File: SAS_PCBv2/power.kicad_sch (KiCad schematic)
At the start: 18 parts, among them J3 Conn_01x02_Pin, Q2 2N4403, Q3 2N4403, SW1 SW_SPST, U2 LF33_TO220

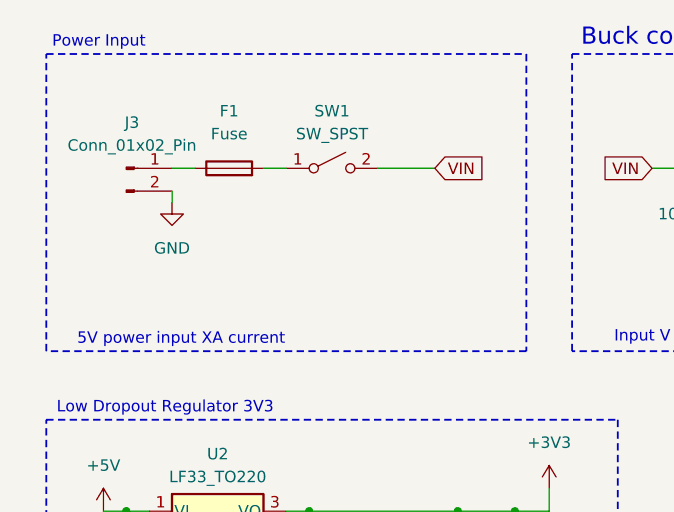
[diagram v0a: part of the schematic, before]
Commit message: Fix footprints, widen power traces, route RPi cables, fix transistor pinout
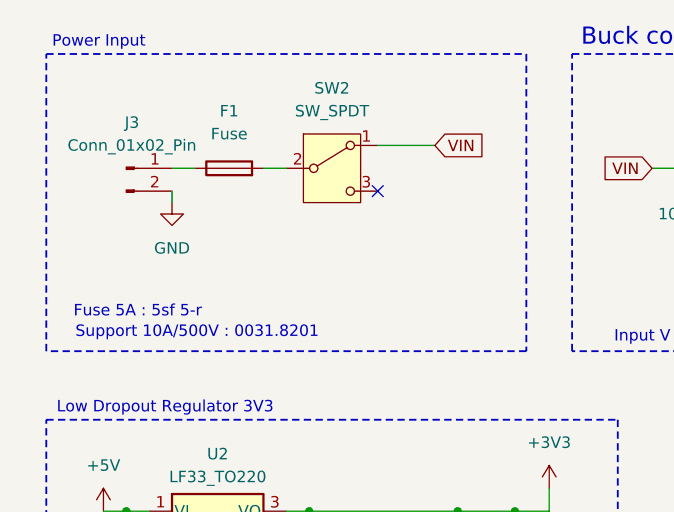
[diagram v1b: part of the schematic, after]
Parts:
- removed SW1: SW_SPST, Button_Switch_THT:SW_DIP_SPSTx01_Piano_10.8x4.1mm_W7.62mm_P2.54mm, symbol Switch:SW_SPST
- added SW2: SW_SPDT, SAS_PCBv2_footprint:SW_ANT1_CRS, symbol Switch:SW_SPDT
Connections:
- net +5V: now also Q3.1 (E); no longer Q3.3 (E)
- net RPI_5V: now also Q2.1 (E); no longer Q2.3 (E)
- net VIN: now also SW2.1 (A)
- net at Q2.2 (B), Q3.2 (B), R10.1: now also Q3.3 (C); no longer Q3.1 (C)
- net at F1.2: now also SW2.2 (B)
- net at MOSFET1.1 (G), R11.1: now also Q2.3 (C); no longer Q2.1 (C)
- no-connect marks 0 -> 1
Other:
- note added: "Fuse 5A : 5sf 5-r"
- note added: "Support 10A/500V : 0031.8201"
- note removed: "5V power input XA current"
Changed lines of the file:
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@@
 		)
 	)
+	(text "Fuse 5A : 5sf 5-r"
+		(exclude_from_sim no)
+		(at 27.94 49.022 0)
+		(effects
+			(font
+				(size 1.27 1.27)
+			)
+		)
+	)
 	(text "Low Dropout Regulator 3V3"
 		(exclude_from_sim no)
@@
 		)
 	)
+	(text "Support 10A/500V : 0031.8201"
+		(exclude_from_sim no)
+		(at 34.544 51.308 0)
+		(effects
+			(font
+				(size 1.27 1.27)
+			)
+		)
+	)
 	(text "Diode idéale (Transistors??)"
 		(exclude_from_sim no)
@@
 		)
 	)
-	(text "5V power input XA current"
-		(exclude_from_sim no)
-		(at 32.766 52.07 0)
-		(effects
-			(font
-				(size 1.27 1.27)
-			)
-		)
-	)
 	(text "Warning:\nModule factory setting is HIGH VOLTAGE.\nDO NOT connect 5V loads (Raspberry Pi/Radio) yet.\n1. Power on board.\n2. Turn blue potentiometer CCW 7-15 turns.\n3. Verify output is exactly 5.0V using the onboard LED display.\n4. Power off, then connect 5V devices."
 		(exclude_from_sim no)
@@
 		(color 0 0 0 0)
 	)
+	(no_connect
+		(at 54.61 35.56)
+	)
 	(wire
 		(pts
@@
 	(wire
 		(pts
-			(xy 54.61 33.02) (xy 60.96 33.02)
+			(xy 54.61 30.48) (xy 60.96 30.48)
 		)
 		(stroke
@@
 	(global_label "VIN"
 		(shape input)
-		(at 60.96 33.02 0)
+		(at 60.96 30.48 0)
 		(fields_autoplaced yes)
 		(effects
@@
 		)
 		(property "Intersheetrefs" "${INTERSHEET_REFS}"
-			(at 66.9691 33.02 0)
+			(at 66.9691 30.48 0)
 			(hide yes)
 			(show_name no)
@@
 	)
 	(symbol
+		(lib_id "Switch:SW_SPDT")
+		(at 49.53 33.02 0)
+		(unit 1)
+		(body_style 1)
+		(exclude_from_sim no)
+		(in_bom yes)
+		(on_board yes)
+		(in_pos_files yes)
+		(dnp no)
+		(fields_autoplaced yes)
+		(property "Reference" "SW2"
+			(at 49.53 24.13 0)
+			(show_name no)
+			(do_not_autoplace no)
+			(effects
+				(font
+					(size 1.27 1.27)
+				)
+			)
+		)
+		(property "Value" "SW_SPDT"
+			(at 49.53 26.67 0)
+			(show_name no)
+			(do_not_autoplace no)
+			(effects
+				(font
+					(size 1.27 1.27)
+				)
+			)
+		)
+		(property "Footprint" "SAS_PCBv2_footprint:SW_ANT1_CRS"
+			(at 49.53 33.02 0)
+			(hide yes)
+			(show_name no)
+			(do_not_autoplace no)
+			(effects
+				(font
+					(size 1.27 1.27)
+				)
+			)
+		)
+		(property "Datasheet" "https://www.citrelay.com/wp-content/uploads/2025/05/Switch-ANT.pdf"
+			(at 49.53 40.64 0)
+			(hide yes)
+			(show_name no)
+			(do_not_autoplace no)
+			(effects
+				(font
+					(size 1.27 1.27)
+				)
+			)
+		)
+		(property "Description" "ANT13SEBQE"
+			(at 49.53 33.02 0)
+			(hide yes)
+			(show_name no)
+			(do_not_autoplace no)
+			(effects
+				(font
+					(size 1.27 1.27)
+				)
+			)
+		)
+		(property "Digikey" "https://www.digikey.ca/en/products/detail/cit-relay-and-switch/ANT13SEBQE/12503275"
+			(at 49.53 33.02 0)
+			(hide yes)
+			(show_name no)
+			(do_not_autoplace no)
+			(effects
+				(font
+					(size 1.27 1.27)
+				)
+			)
+		)
+		(pin "3"
+		)
+		(pin "2"
+		)
+		(pin "1"
+		)
+		(instances
+			(project "SAS_PCBv2"
+				(path "/9d66b581-dc57-43dc-b827-73e5c0cd12f6/3d73fe98-5b95-4bdf-b7ce-5bce46366f48"
+					(reference "SW2")
+					(unit 1)
+				)
+			)
+		)
+	)
+	(symbol
 		(lib_id "power:GND")
 		(at 100.33 41.91 0)
@@
 	)
 	(symbol
+		(lib_name "PNP_1")
 		(lib_id "Simulation_SPICE:PNP")
 		(at 38.1 128.27 180)
@@
 			)
 		)
-		(property "Datasheet" "https://diotec.com/request/datasheet/2n4403.pdf"
+		(property "Datasheet" "https://my.centralsemi.com/datasheets/2N4402.PDF"
 			(at 2.54 128.27 0)
 			(hide yes)
@@
 			)
 		)
-		(property "Sim.Pins" "1=C 2=B 3=E"
+		(property "Sim.Pins" "1=E 2=B 3=C"
 			(at 38.1 128.27 0)
 			(hide yes)
@@
 	)
 	(symbol
-		(lib_id "Switch:SW_SPST")
-		(at 49.53 33.02 0)
-		(unit 1)
-		(body_style 1)
-		(exclude_from_sim no)
-		(in_bom yes)
-		(on_board yes)
-		(in_pos_files yes)
-		(dnp no)
-		(fields_autoplaced yes)
-		(property "Reference" "SW1"
-			(at 49.53 26.67 0)
-			(show_name no)
-			(do_not_autoplace no)
-			(effects
-				(font
-					(size 1.27 1.27)
-				)
-			)
-		)
-		(property "Value" "SW_SPST"
-			(at 49.53 29.21 0)
-			(show_name no)
-			(do_not_autoplace no)
-			(effects
-				(font
-					(size 1.27 1.27)
-				)
-			)
-		)
-		(property "Footprint" "Button_Switch_THT:SW_DIP_SPSTx01_Piano_10.8x4.1mm_W7.62mm_P2.54mm"
-			(at 49.53 33.02 0)
-			(hide yes)
-			(show_name no)
-			(do_not_autoplace no)
-			(effects
-				(font
-					(size 1.27 1.27)
-				)
-			)
-		)
-		(property "Datasheet" ""
-			(at 49.53 33.02 0)
-			(hide yes)
-			(show_name no)
-			(do_not_autoplace no)
-			(effects
-				(font
-					(size 1.27 1.27)
-				)
-			)
-		)
-		(property "Description" "Single Pole Single Throw (SPST) switch"
-			(at 49.53 33.02 0)
-			(hide yes)
-			(show_name no)
-			(do_not_autoplace no)
-			(effects
-				(font
-					(size 1.27 1.27)
-				)
-			)
-		)
-		(property "AVAILABILITY" ""
-			(at 49.53 33.02 0)
-			(hide yes)
-			(show_name no)
-			(do_not_autoplace no)
-			(effects
-				(font
-					(size 1.27 1.27)
-				)
-			)
-		)
-		(property "Digikey" ""
-			(at 49.53 33.02 0)
-			(hide yes)
-			(show_name no)
-			(do_not_autoplace no)
-			(effects
-				(font
-					(size 1.27 1.27)
-				)
-			)
-		)
-		(property "MF" ""
-			(at 49.53 33.02 0)
-			(hide yes)
-			(show_name no)
-			(do_not_autoplace no)
-			(effects
-				(font
-					(size 1.27 1.27)
-				)
-			)
-		)
-		(property "MP" ""
-			(at 49.53 33.02 0)
-			(hide yes)
-			(show_name no)
-			(do_not_autoplace no)
-			(effects
-				(font
-					(size 1.27 1.27)
-				)
-			)
-		)
-		(property "PACKAGE" ""
-			(at 49.53 33.02 0)
-			(hide yes)
-			(show_name no)
-			(do_not_autoplace no)
-			(effects
-				(font
-					(size 1.27 1.27)
-				)
-			)
-		)
-		(property "PRICE" ""
-			(at 49.53 33.02 0)
-			(hide yes)
-			(show_name no)
-			(do_not_autoplace no)
-			(effects
-				(font
-					(size 1.27 1.27)
-				)
-			)
-		)
-		(property "PURCHASE-URL" ""
-			(at 49.53 33.02 0)
-			(hide yes)
-			(show_name no)
-			(do_not_autoplace no)
-			(effects
-				(font
-					(size 1.27 1.27)
-				)
-			)
-		)
-		(pin "2"
-		)
-		(pin "1"
-		)
-		(instances
-			(project "SAS_PCBv2"
-				(path "/9d66b581-dc57-43dc-b827-73e5c0cd12f6/3d73fe98-5b95-4bdf-b7ce-5bce46366f48"
-					(reference "SW1")
-					(unit 1)
-				)
-			)
-		)
-	)
-	(symbol
 		(lib_id "Simulation_SPICE:PNP")
 		(at 53.34 128.27 0)
@@
 			)
 		)
-		(property "Datasheet" "https://diotec.com/request/datasheet/2n4403.pdf"
+		(property "Datasheet" "https://my.centralsemi.com/datasheets/2N4402.PDF"
 			(at 88.9 128.27 0)
 			(hide yes)
@@
 			)
 		)
-		(property "Sim.Pins" "1=C 2=B 3=E"
+		(property "Sim.Pins" "1=E 2=B 3=C"
 			(at 53.34 128.27 0)
 			(hide yes)

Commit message: finition et fabrication
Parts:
- J3: footprint Connector_PinHeader_2.54mm:PinHeader_1x02_P2.54mm_Vertical -> Connector_AMASS:AMASS_XT30U-M_1x02_P5.0mm_Vertical
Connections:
- net GND: now also J3.1 (Pin_1); no longer J3.2 (Pin_2)
- net at F1.1: now also J3.2 (Pin_2); no longer J3.1 (Pin_1)
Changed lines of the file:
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@@
 	(wire
 		(pts
+			(xy 31.75 33.02) (xy 34.29 33.02)
+		)
+		(stroke
+			(width 0)
+			(type default)
+		)
+	)
+	(wire
+		(pts
 			(xy 31.75 113.03) (xy 31.75 116.84)
 		)
@@
 	(wire
 		(pts
+			(xy 31.75 35.56) (xy 31.75 36.83)
+		)
+		(stroke
+			(width 0)
+			(type default)
+		)
+	)
+	(wire
+		(pts
 			(xy 59.69 113.03) (xy 59.69 116.84)
 		)
@@
 	(wire
 		(pts
-			(xy 31.75 33.02) (xy 34.29 33.02)
-		)
-		(stroke
-			(width 0)
-			(type default)
-		)
-	)
-	(wire
-		(pts
 			(xy 31.75 116.84) (xy 22.86 116.84)
 		)
@@
 	(wire
 		(pts
-			(xy 31.75 35.56) (xy 31.75 36.83)
-		)
-		(stroke
-			(width 0)
-			(type default)
-		)
-	)
-	(wire
-		(pts
 			(xy 69.85 78.74) (xy 69.85 80.01)
 		)
@@
 	(symbol
 		(lib_id "Connector:Conn_01x02_Pin")
-		(at 26.67 33.02 0)
+		(at 26.67 35.56 0)
+		(mirror x)
 		(unit 1)
 		(body_style 1)
@@
 		(in_pos_files yes)
 		(dnp no)
-		(fields_autoplaced yes)
 		(property "Reference" "J3"
-			(at 27.305 27.94 0)
+			(at 24.638 34.29 0)
 			(show_name no)
 			(do_not_autoplace no)
@@
 		)
 		(property "Value" "Conn_01x02_Pin"
-			(at 27.305 30.48 0)
+			(at 26.162 29.464 0)
 			(show_name no)
 			(do_not_autoplace no)
@@
 			)
 		)
-		(property "Footprint" "Connector_PinHeader_2.54mm:PinHeader_1x02_P2.54mm_Vertical"
-			(at 26.67 33.02 0)
+		(property "Footprint" "Connector_AMASS:AMASS_XT30U-M_1x02_P5.0mm_Vertical"
+			(at 26.67 35.56 0)
 			(hide yes)
 			(show_name no)
@@
 		)
 		(property "Datasheet" ""
-			(at 26.67 33.02 0)
+			(at 26.67 35.56 0)
 			(hide yes)
 			(show_name no)
@@
 			)
 		)
-		(property "Description" "Generic connector, single row, 01x02, script generated"
-			(at 26.67 33.02 0)
+		(property "Description" "xt30"
+			(at 26.67 35.56 0)
 			(hide yes)
 			(show_name no)
@@
 		)
 		(property "AVAILABILITY" ""
-			(at 26.67 33.02 0)
+			(at 26.67 35.56 0)
 			(hide yes)
 			(show_name no)
@@
 		)
 		(property "Digikey" ""
-			(at 26.67 33.02 0)
+			(at 26.67 35.56 0)
 			(hide yes)
 			(show_name no)
@@
 		)
 		(property "MF" ""
-			(at 26.67 33.02 0)
+			(at 26.67 35.56 0)
 			(hide yes)
 			(show_name no)
@@
 		)
 		(property "MP" ""
-			(at 26.67 33.02 0)
+			(at 26.67 35.56 0)
 			(hide yes)
 			(show_name no)
@@
 		)
 		(property "PACKAGE" ""
-			(at 26.67 33.02 0)
+			(at 26.67 35.56 0)
 			(hide yes)
 			(show_name no)
@@
 		)
 		(property "PRICE" ""
-			(at 26.67 33.02 0)
+			(at 26.67 35.56 0)
 			(hide yes)
 			(show_name no)
@@
 		)
 		(property "PURCHASE-URL" ""
-			(at 26.67 33.02 0)
+			(at 26.67 35.56 0)
 			(hide yes)
 			(show_name no)
